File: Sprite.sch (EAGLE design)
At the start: 24 parts, among them P1 SPRITE_PIN, P2 SPRITE_PIN, U1 CC430F5137, X1 TCXO_7Z

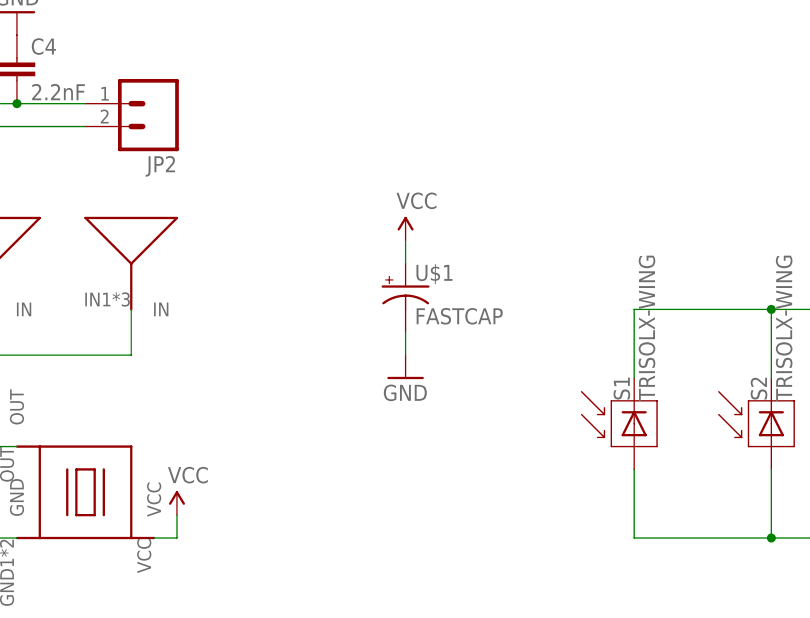
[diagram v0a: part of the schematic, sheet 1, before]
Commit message: Added murata UMAC battery
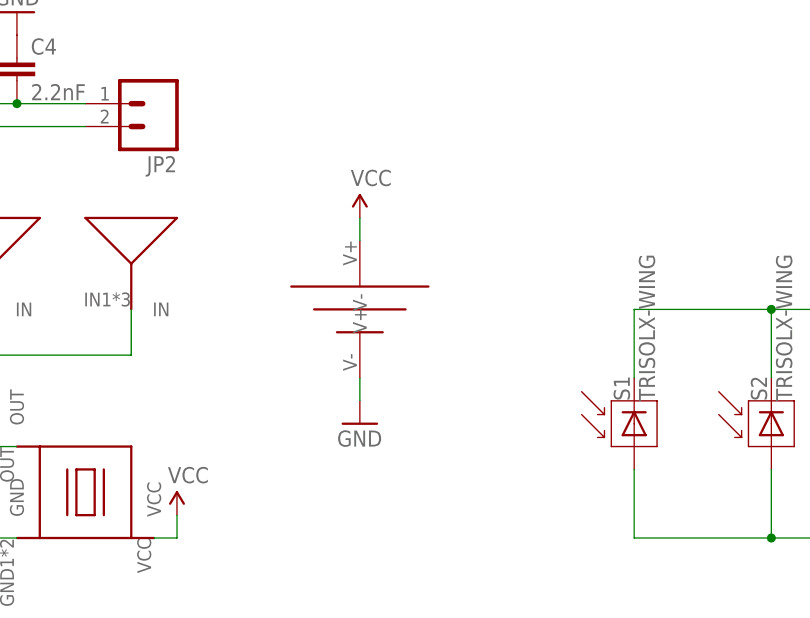
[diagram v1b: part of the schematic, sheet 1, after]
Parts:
- U$1: value FASTCAP -> UMAC; device FastCap:FASTCAP -> UMAC:UMAC
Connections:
- net GND: now also U$1.V-; no longer U$1.-
- net VCC: now also U$1.V+; no longer U$1.+
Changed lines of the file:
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@@
 <?xml version="1.0" encoding="utf-8"?>
 <!DOCTYPE eagle SYSTEM "eagle.dtd">
-<eagle version="8.6.1">
+<eagle version="9.0.0">
 <drawing>
 <settings>
@@
 <layer number="2" name="Route2" color="1" fill="3" visible="no" active="no"/>
 <layer number="3" name="Route3" color="4" fill="3" visible="no" active="no"/>
+<layer number="4" name="Route4" color="1" fill="4" visible="no" active="no"/>
+<layer number="5" name="Route5" color="4" fill="4" visible="no" active="no"/>
+<layer number="6" name="Route6" color="1" fill="8" visible="no" active="no"/>
+<layer number="7" name="Route7" color="4" fill="8" visible="no" active="no"/>
+<layer number="8" name="Route8" color="1" fill="2" visible="no" active="no"/>
+<layer number="9" name="Route9" color="4" fill="2" visible="no" active="no"/>
+<layer number="10" name="Route10" color="1" fill="7" visible="no" active="no"/>
+<layer number="11" name="Route11" color="4" fill="7" visible="no" active="no"/>
+<layer number="12" name="Route12" color="1" fill="5" visible="no" active="no"/>
+<layer number="13" name="Route13" color="4" fill="5" visible="no" active="no"/>
 <layer number="14" name="Route14" color="1" fill="6" visible="no" active="no"/>
 <layer number="15" name="Route15" color="4" fill="6" visible="no" active="no"/>
@@
 <part name="P+11" library="SparkFun" deviceset="VCC" device=""/>
 <part name="GND7" library="SparkFun" deviceset="GND" device=""/>
-<part name="U$1" library="FastCap" deviceset="FASTCAP" device=""/>
 <part name="P+3" library="SparkFun" deviceset="VCC" device=""/>
 <part name="GND9" library="SparkFun" deviceset="GND" device=""/>
+<part name="U$1" library="UMAC" deviceset="UMAC" device=""/>
 </parts>
 <sheets>
@@
 <instance part="P+11" gate="1" x="132.08" y="-5.08"/>
 <instance part="GND7" gate="1" x="86.36" y="20.32"/>
-<instance part="U$1" gate="G$1" x="157.48" y="20.32"/>
-<instance part="P+3" gate="1" x="157.48" y="25.4"/>
-<instance part="GND9" gate="1" x="157.48" y="10.16"/>
+<instance part="P+3" gate="1" x="152.4" y="27.94"/>
+<instance part="GND9" gate="1" x="152.4" y="5.08"/>
+<instance part="U$1" gate="G$1" x="152.4" y="17.78"/>
 </instances>
 <busses>
@@
 </segment>
 <segment>
-<pinref part="U$1" gate="G$1" pin="+"/>
+<pinref part="U$1" gate="G$1" pin="V+"/>
 <pinref part="P+3" gate="1" pin="VCC"/>
-<wire x1="157.48" y1="22.86" x2="157.48" y2="25.4" width="0.1524" layer="91"/>
+<wire x1="152.4" y1="25.4" x2="152.4" y2="27.94" width="0.1524" layer="91"/>
 </segment>
 </net>
@@
 <segment>
 <pinref part="GND9" gate="1" pin="GND"/>
-<pinref part="U$1" gate="G$1" pin="-"/>
-<wire x1="157.48" y1="12.7" x2="157.48" y2="15.24" width="0.1524" layer="91"/>
+<pinref part="U$1" gate="G$1" pin="V-"/>
+<wire x1="152.4" y1="7.62" x2="152.4" y2="10.16" width="0.1524" layer="91"/>
 </segment>
 </net>
